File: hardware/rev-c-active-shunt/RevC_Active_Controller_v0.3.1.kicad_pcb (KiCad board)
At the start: 2 copper layers, 60 x 40 mm, 25 parts, among them J1 TEST_A / GND, J2 +12/GND/-12, U1 OPA551PA

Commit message: Rev.C v0.3.1: reroute power and ground to clear DRC
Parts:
- moved C107 3.00 mm to (17.0, 26.0)
- moved C105 2.00 mm to (45.0, 17.0)
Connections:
- U1 pad 1: (no net) -> unconnected-(U1-NC-Pad1)
- U1 pad 5: (no net) -> unconnected-(U1-NC-Pad5)
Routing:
- net /GND: track 86.7 -> 130.2 mm
- net /-12V: track 52.5 -> 73.8 mm
- net /OUT: track 29.4 -> 21.6 mm
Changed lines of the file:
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@@
   (net 10 "/BOOST_SW")
   (net 11 "/FLAG")
+  (net 12 "unconnected-(U1-NC-Pad1)")
+  (net 13 "unconnected-(U1-NC-Pad5)")
   (footprint "RevC:Terminal_2P_5.08" (layer "F.Cu")
     (at 5.00 20.00)
@@
     (fp_text reference "U1" (at 0 -3) (layer "F.SilkS") (effects (font (size 1 1) (thickness 0.15))))
     (fp_text value "OPA551PA" (at 0 3) (layer "F.Fab") hide (effects (font (size 0.8 0.8) (thickness 0.12))))
-    (pad "1" thru_hole rect (at -3.81 -3.81) (size 1.80 1.80) (drill 0.90) (layers "*.Cu" "*.Mask"))
+    (pad "1" thru_hole rect (at -3.81 -3.81) (size 1.80 1.80) (drill 0.90) (layers "*.Cu" "*.Mask") (net 12 "unconnected-(U1-NC-Pad1)"))
     (pad "2" thru_hole circle (at -3.81 -1.27) (size 1.80 1.80) (drill 0.90) (layers "*.Cu" "*.Mask") (net 6 "/NINV"))
     (pad "3" thru_hole circle (at -3.81 1.27) (size 1.80 1.80) (drill 0.90) (layers "*.Cu" "*.Mask") (net 2 "/GND"))
     (pad "4" thru_hole circle (at -3.81 3.81) (size 1.80 1.80) (drill 0.90) (layers "*.Cu" "*.Mask") (net 4 "/-12V"))
-    (pad "5" thru_hole circle (at 3.81 3.81) (size 1.80 1.80) (drill 0.90) (layers "*.Cu" "*.Mask"))
+    (pad "5" thru_hole circle (at 3.81 3.81) (size 1.80 1.80) (drill 0.90) (layers "*.Cu" "*.Mask") (net 13 "unconnected-(U1-NC-Pad5)"))
     (pad "6" thru_hole circle (at 3.81 1.27) (size 1.80 1.80) (drill 0.90) (layers "*.Cu" "*.Mask") (net 7 "/OUT"))
     (pad "7" thru_hole circle (at 3.81 -1.27) (size 1.80 1.80) (drill 0.90) (layers "*.Cu" "*.Mask") (net 3 "/+12V"))
@@
   )
   (footprint "Capacitor_SMD:C_1206_3216Metric" (layer "F.Cu")
-    (at 43.00 17.00)
+    (at 45.00 17.00)
     (attr smd)
     (fp_text reference "C105" (at 0 -3) (layer "F.SilkS") (effects (font (size 1 1) (thickness 0.15))))
@@
   )
   (footprint "Capacitor_SMD:C_1206_3216Metric" (layer "F.Cu")
-    (at 20.00 26.00)
+    (at 17.00 26.00)
     (attr smd)
     (fp_text reference "C107" (at 0 -3) (layer "F.SilkS") (effects (font (size 1 1) (thickness 0.15))))
@@
   (segment (start 30.00 10.00) (end 30.00 13.00) (width 0.30) (layer "F.Cu") (net 6))
   (segment (start 30.00 13.00) (end 30.00 15.00) (width 0.30) (layer "F.Cu") (net 6))
-  (segment (start 34.81 21.27) (end 36.00 21.27) (width 0.50) (layer "F.Cu") (net 7))
-  (segment (start 36.00 21.27) (end 36.00 10.00) (width 0.30) (layer "F.Cu") (net 7))
-  (segment (start 36.00 10.00) (end 32.00 10.00) (width 0.30) (layer "F.Cu") (net 7))
-  (segment (start 32.00 10.00) (end 32.00 13.00) (width 0.30) (layer "F.Cu") (net 7))
+  (segment (start 34.81 21.27) (end 33.00 21.27) (width 0.50) (layer "F.Cu") (net 7))
+  (segment (start 33.00 21.27) (end 33.00 17.00) (width 0.30) (layer "F.Cu") (net 7))
+  (segment (start 33.00 17.00) (end 32.00 17.00) (width 0.30) (layer "F.Cu") (net 7))
+  (segment (start 32.00 17.00) (end 32.00 13.00) (width 0.30) (layer "F.Cu") (net 7))
   (segment (start 32.00 13.00) (end 32.00 15.00) (width 0.30) (layer "F.Cu") (net 7))
-  (segment (start 36.00 21.27) (end 37.00 24.00) (width 0.50) (layer "F.Cu") (net 7))
+  (segment (start 34.81 21.27) (end 37.00 24.00) (width 0.50) (layer "F.Cu") (net 7))
   (segment (start 37.00 24.00) (end 37.50 29.00) (width 0.60) (layer "F.Cu") (net 7))
   (segment (start 42.50 29.00) (end 44.00 29.00) (width 0.80) (layer "F.Cu") (net 8))
@@
   (segment (start 46.00 18.73) (end 34.81 18.73) (width 0.80) (layer "F.Cu") (net 3))
   (segment (start 38.00 17.00) (end 38.00 18.73) (width 0.50) (layer "F.Cu") (net 3))
-  (segment (start 41.50 17.00) (end 41.50 18.73) (width 0.50) (layer "F.Cu") (net 3))
-  (segment (start 55.00 25.08) (end 50.00 25.08) (width 0.80) (layer "F.Cu") (net 4))
-  (segment (start 50.00 25.08) (end 50.00 28.00) (width 0.80) (layer "F.Cu") (net 4))
-  (segment (start 50.00 25.08) (end 46.00 25.08) (width 0.80) (layer "F.Cu") (net 4))
-  (segment (start 46.00 25.08) (end 46.00 31.00) (width 0.80) (layer "F.Cu") (net 4))
-  (segment (start 46.00 31.00) (end 27.19 31.00) (width 0.80) (layer "F.Cu") (net 4))
-  (segment (start 27.19 31.00) (end 27.19 23.81) (width 0.80) (layer "F.Cu") (net 4))
-  (segment (start 27.19 26.00) (end 23.00 26.00) (width 0.50) (layer "F.Cu") (net 4))
-  (segment (start 23.00 26.00) (end 18.50 26.00) (width 0.50) (layer "F.Cu") (net 4))
+  (segment (start 43.50 17.00) (end 43.50 18.73) (width 0.50) (layer "F.Cu") (net 3))
+  (segment (start 27.19 23.81) (end 27.19 36.00) (width 0.80) (layer "B.Cu") (net 4))
+  (segment (start 27.19 36.00) (end 50.00 36.00) (width 0.80) (layer "B.Cu") (net 4))
+  (segment (start 50.00 36.00) (end 50.00 25.08) (width 0.80) (layer "B.Cu") (net 4))
+  (segment (start 50.00 25.08) (end 55.00 25.08) (width 0.80) (layer "B.Cu") (net 4))
+  (segment (start 27.19 23.81) (end 27.19 29.00) (width 0.50) (layer "F.Cu") (net 4))
+  (segment (start 27.19 29.00) (end 23.00 29.00) (width 0.50) (layer "F.Cu") (net 4))
+  (segment (start 23.00 29.00) (end 23.00 26.00) (width 0.50) (layer "F.Cu") (net 4))
+  (segment (start 23.00 29.00) (end 15.50 29.00) (width 0.50) (layer "F.Cu") (net 4))
+  (segment (start 15.50 29.00) (end 15.50 26.00) (width 0.50) (layer "F.Cu") (net 4))
   (via (at 40.00 17.00) (size 1.0) (drill 0.5) (layers "F.Cu" "B.Cu") (net 2))
-  (via (at 44.50 17.00) (size 1.0) (drill 0.5) (layers "F.Cu" "B.Cu") (net 2))
+  (via (at 46.50 17.00) (size 1.0) (drill 0.5) (layers "F.Cu" "B.Cu") (net 2))
   (via (at 25.00 26.00) (size 1.0) (drill 0.5) (layers "F.Cu" "B.Cu") (net 2))
-  (via (at 21.50 26.00) (size 1.0) (drill 0.5) (layers "F.Cu" "B.Cu") (net 2))
+  (via (at 18.50 26.00) (size 1.0) (drill 0.5) (layers "F.Cu" "B.Cu") (net 2))
   (via (at 42.00 10.00) (size 1.0) (drill 0.5) (layers "F.Cu" "B.Cu") (net 2))
-  (segment (start 5.00 22.54) (end 27.19 21.27) (width 0.80) (layer "B.Cu") (net 2))
-  (segment (start 27.19 21.27) (end 50.00 20.00) (width 0.80) (layer "B.Cu") (net 2))
-  (segment (start 50.00 20.00) (end 55.00 20.00) (width 0.80) (layer "B.Cu") (net 2))
-  (segment (start 21.50 26.00) (end 27.19 21.27) (width 0.50) (layer "B.Cu") (net 2))
-  (segment (start 25.00 26.00) (end 27.19 21.27) (width 0.50) (layer "B.Cu") (net 2))
-  (segment (start 40.00 17.00) (end 50.00 20.00) (width 0.50) (layer "B.Cu") (net 2))
-  (segment (start 44.50 17.00) (end 50.00 20.00) (width 0.50) (layer "B.Cu") (net 2))
-  (segment (start 42.00 10.00) (end 40.00 17.00) (width 0.50) (layer "B.Cu") (net 2))
+  (segment (start 5.00 22.54) (end 20.00 22.54) (width 0.80) (layer "B.Cu") (net 2))
+  (segment (start 20.00 22.54) (end 20.00 21.27) (width 0.80) (layer "B.Cu") (net 2))
+  (segment (start 20.00 21.27) (end 27.19 21.27) (width 0.80) (layer "B.Cu") (net 2))
+  (segment (start 27.19 21.27) (end 22.00 21.27) (width 0.80) (layer "B.Cu") (net 2))
+  (segment (start 22.00 21.27) (end 22.00 6.00) (width 0.80) (layer "B.Cu") (net 2))
+  (segment (start 22.00 6.00) (end 52.00 6.00) (width 0.80) (layer "B.Cu") (net 2))
+  (segment (start 52.00 6.00) (end 52.00 20.00) (width 0.80) (layer "B.Cu") (net 2))
+  (segment (start 52.00 20.00) (end 55.00 20.00) (width 0.80) (layer "B.Cu") (net 2))
+  (segment (start 50.00 20.00) (end 52.00 20.00) (width 0.80) (layer "B.Cu") (net 2))
+  (segment (start 18.50 26.00) (end 20.00 26.00) (width 0.50) (layer "B.Cu") (net 2))
+  (segment (start 25.00 26.00) (end 20.00 26.00) (width 0.50) (layer "B.Cu") (net 2))
+  (segment (start 20.00 26.00) (end 20.00 21.27) (width 0.50) (layer "B.Cu") (net 2))
+  (segment (start 40.00 17.00) (end 40.00 6.00) (width 0.50) (layer "B.Cu") (net 2))
+  (segment (start 46.50 17.00) (end 46.50 6.00) (width 0.50) (layer "B.Cu") (net 2))
+  (segment (start 42.00 10.00) (end 42.00 6.00) (width 0.50) (layer "B.Cu") (net 2))
 )

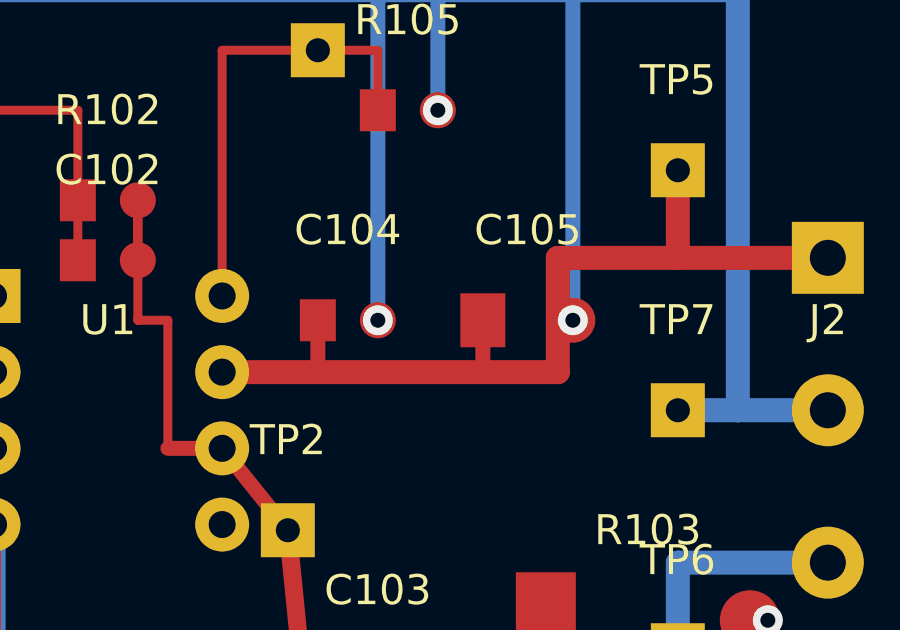
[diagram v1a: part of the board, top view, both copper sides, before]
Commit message: Rev.C v0.3.1: clear final +12V DRC and TP parity
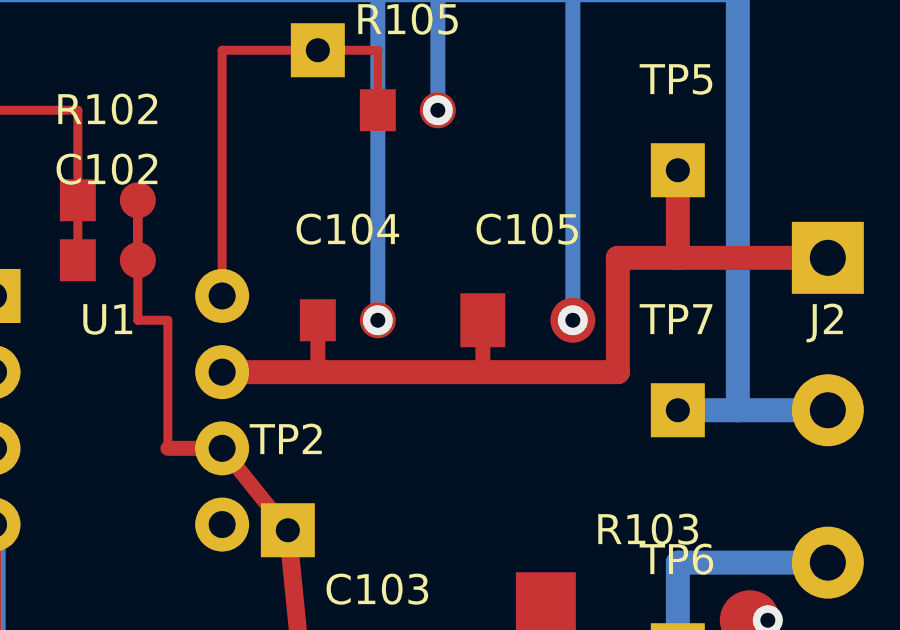
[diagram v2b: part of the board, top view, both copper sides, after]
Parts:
- TP1: value /TEST_A -> TP1
- TP2: value /OUT -> TP2
- TP3: value /NINV -> TP3
- TP4: value /INJ_NODE -> TP4
- TP5: value /+12V -> TP5
- TP6: value /-12V -> TP6
- TP7: value /GND -> TP7
- TP8: value /FLAG -> TP8
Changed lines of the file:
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@@
     (attr through_hole)
     (fp_text reference "TP1" (at 0 -3) (layer "F.SilkS") (effects (font (size 1 1) (thickness 0.15))))
-    (fp_text value "/TEST_A" (at 0 3) (layer "F.Fab") hide (effects (font (size 0.8 0.8) (thickness 0.12))))
+    (fp_text value "TP1" (at 0 3) (layer "F.Fab") hide (effects (font (size 0.8 0.8) (thickness 0.12))))
     (pad "1" thru_hole rect (at 0.00 0.00) (size 1.80 1.80) (drill 0.80) (layers "*.Cu" "*.Mask") (net 1 "/TEST_A"))
   )
@@
     (attr through_hole)
     (fp_text reference "TP2" (at 0 -3) (layer "F.SilkS") (effects (font (size 1 1) (thickness 0.15))))
-    (fp_text value "/OUT" (at 0 3) (layer "F.Fab") hide (effects (font (size 0.8 0.8) (thickness 0.12))))
+    (fp_text value "TP2" (at 0 3) (layer "F.Fab") hide (effects (font (size 0.8 0.8) (thickness 0.12))))
     (pad "1" thru_hole rect (at 0.00 0.00) (size 1.80 1.80) (drill 0.80) (layers "*.Cu" "*.Mask") (net 7 "/OUT"))
   )
@@
     (attr through_hole)
     (fp_text reference "TP3" (at 0 -3) (layer "F.SilkS") (effects (font (size 1 1) (thickness 0.15))))
-    (fp_text value "/NINV" (at 0 3) (layer "F.Fab") hide (effects (font (size 0.8 0.8) (thickness 0.12))))
+    (fp_text value "TP3" (at 0 3) (layer "F.Fab") hide (effects (font (size 0.8 0.8) (thickness 0.12))))
     (pad "1" thru_hole rect (at 0.00 0.00) (size 1.80 1.80) (drill 0.80) (layers "*.Cu" "*.Mask") (net 6 "/NINV"))
   )
@@
     (attr through_hole)
     (fp_text reference "TP4" (at 0 -3) (layer "F.SilkS") (effects (font (size 1 1) (thickness 0.15))))
-    (fp_text value "/INJ_NODE" (at 0 3) (layer "F.Fab") hide (effects (font (size 0.8 0.8) (thickness 0.12))))
+    (fp_text value "TP4" (at 0 3) (layer "F.Fab") hide (effects (font (size 0.8 0.8) (thickness 0.12))))
     (pad "1" thru_hole rect (at 0.00 0.00) (size 1.80 1.80) (drill 0.80) (layers "*.Cu" "*.Mask") (net 8 "/INJ_NODE"))
   )
@@
     (attr through_hole)
     (fp_text reference "TP5" (at 0 -3) (layer "F.SilkS") (effects (font (size 1 1) (thickness 0.15))))
-    (fp_text value "/+12V" (at 0 3) (layer "F.Fab") hide (effects (font (size 0.8 0.8) (thickness 0.12))))
+    (fp_text value "TP5" (at 0 3) (layer "F.Fab") hide (effects (font (size 0.8 0.8) (thickness 0.12))))
     (pad "1" thru_hole rect (at 0.00 0.00) (size 1.80 1.80) (drill 0.80) (layers "*.Cu" "*.Mask") (net 3 "/+12V"))
   )
@@
     (attr through_hole)
     (fp_text reference "TP6" (at 0 -3) (layer "F.SilkS") (effects (font (size 1 1) (thickness 0.15))))
-    (fp_text value "/-12V" (at 0 3) (layer "F.Fab") hide (effects (font (size 0.8 0.8) (thickness 0.12))))
+    (fp_text value "TP6" (at 0 3) (layer "F.Fab") hide (effects (font (size 0.8 0.8) (thickness 0.12))))
     (pad "1" thru_hole rect (at 0.00 0.00) (size 1.80 1.80) (drill 0.80) (layers "*.Cu" "*.Mask") (net 4 "/-12V"))
   )
@@
     (attr through_hole)
     (fp_text reference "TP7" (at 0 -3) (layer "F.SilkS") (effects (font (size 1 1) (thickness 0.15))))
-    (fp_text value "/GND" (at 0 3) (layer "F.Fab") hide (effects (font (size 0.8 0.8) (thickness 0.12))))
+    (fp_text value "TP7" (at 0 3) (layer "F.Fab") hide (effects (font (size 0.8 0.8) (thickness 0.12))))
     (pad "1" thru_hole rect (at 0.00 0.00) (size 1.80 1.80) (drill 0.80) (layers "*.Cu" "*.Mask") (net 2 "/GND"))
   )
@@
     (attr through_hole)
     (fp_text reference "TP8" (at 0 -3) (layer "F.SilkS") (effects (font (size 1 1) (thickness 0.15))))
-    (fp_text value "/FLAG" (at 0 3) (layer "F.Fab") hide (effects (font (size 0.8 0.8) (thickness 0.12))))
+    (fp_text value "TP8" (at 0 3) (layer "F.Fab") hide (effects (font (size 0.8 0.8) (thickness 0.12))))
     (pad "1" thru_hole rect (at 0.00 0.00) (size 1.80 1.80) (drill 0.80) (layers "*.Cu" "*.Mask") (net 11 "/FLAG"))
   )
@@
   (segment (start 55.00 14.92) (end 50.00 14.92) (width 0.80) (layer "F.Cu") (net 3))
   (segment (start 50.00 14.92) (end 50.00 12.00) (width 0.80) (layer "F.Cu") (net 3))
-  (segment (start 50.00 14.92) (end 46.00 14.92) (width 0.80) (layer "F.Cu") (net 3))
-  (segment (start 46.00 14.92) (end 46.00 18.73) (width 0.80) (layer "F.Cu") (net 3))
-  (segment (start 46.00 18.73) (end 34.81 18.73) (width 0.80) (layer "F.Cu") (net 3))
+  (segment (start 50.00 14.92) (end 48.00 14.92) (width 0.80) (layer "F.Cu") (net 3))
+  (segment (start 48.00 14.92) (end 48.00 18.73) (width 0.80) (layer "F.Cu") (net 3))
+  (segment (start 48.00 18.73) (end 34.81 18.73) (width 0.80) (layer "F.Cu") (net 3))
   (segment (start 38.00 17.00) (end 38.00 18.73) (width 0.50) (layer "F.Cu") (net 3))
   (segment (start 43.50 17.00) (end 43.50 18.73) (width 0.50) (layer "F.Cu") (net 3))
